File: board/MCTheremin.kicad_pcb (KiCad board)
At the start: 2 copper layers, 100 x 100 mm, 94 parts, among them J1 Barrel_Jack, J11 Conn_01x01, J12 Conn_01x01, J14 Conn_01x01, J15 Conn_01x01, J2 Conn_01x02, J21 DIN-5_180degree, J3 AudioJack2_Dual_Ground_Switch, J4 AudioJack2_Dual_Ground_Switch, J5 Conn_01x02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

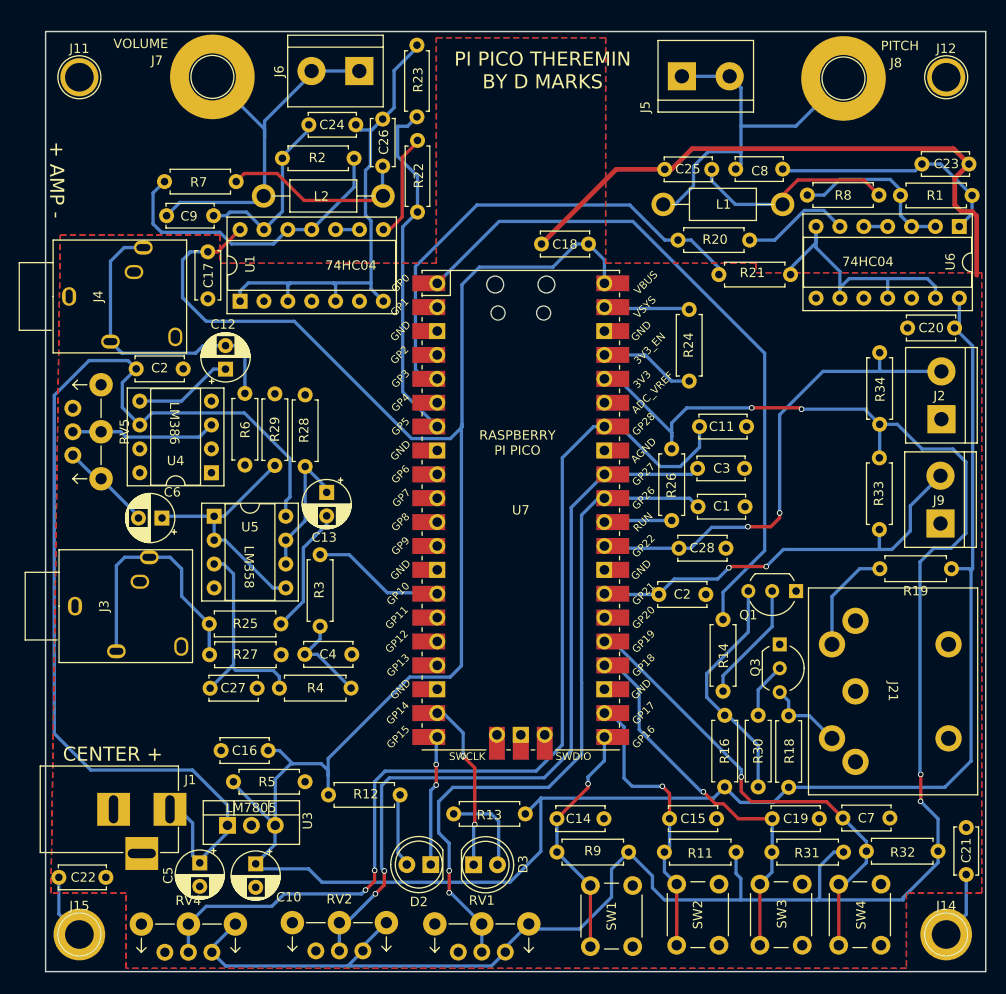
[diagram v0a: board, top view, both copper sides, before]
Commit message: Added external inductor support
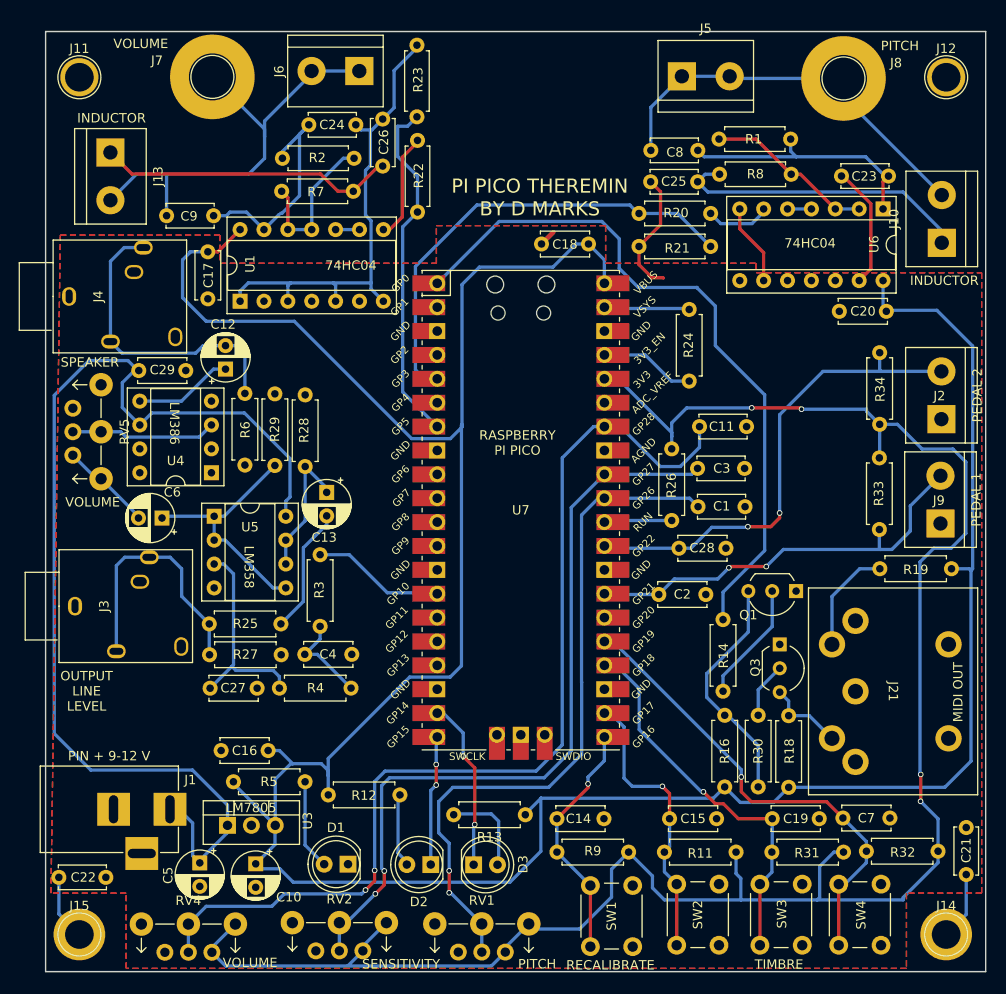
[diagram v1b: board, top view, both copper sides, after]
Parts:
- removed the C2 at (59.6, 85.9)
- removed L1, L2: 400 uH, Inductors_THT:L_Axial_L7.0mm_D3.3mm_P12.70mm_Horizontal_Fastron_MICC
- added C29: 100 nF, Capacitor_THT:C_Disc_D5.0mm_W2.5mm_P5.00mm, F.Cu at (59.9, 86.1)
- added D1: LED, LED_THT:LED_D5.0mm, F.Cu at (82.2, 138.6)
- added J10: Conn_01x02, TerminalBlock:TerminalBlock_bornier-2_P5.08mm, F.Cu at (145.3, 72.5)
- added J13: Conn_01x02, TerminalBlock:TerminalBlock_bornier-2_P5.08mm, F.Cu at (56.9, 62.9)
- J5: footprint Connectors_Terminal_Blocks:TerminalBlock_bornier-2_P5.08mm -> TerminalBlock:TerminalBlock_bornier-2_P5.08mm
- R12, R13, R5: footprint Resistors_THT:R_Axial_DIN0207_L6.3mm_D2.5mm_P7.62mm_Horizontal -> Resistor_THT:R_Axial_DIN0207_L6.3mm_D2.5mm_P7.62mm_Horizontal
- moved R1 20.2 mm to (121.6, 61.4)
- moved R7 12.5 mm to (75.1, 67.0)
- moved C8 9.25 mm to (119.4, 62.6)
- moved U6 8.32 mm to (139.1, 68.9)
- moved C20 7.47 mm to (139.4, 79.8)
- moved R20 5.03 mm to (120.7, 69.4)
- moved C23 3.78 mm to (139.7, 65.4), turned to 180 degrees
- moved R21 3.12 mm to (120.7, 72.9), turned to 180 degrees
- moved R8 2.80 mm to (129.3, 65.2), turned to 180 degrees
- moved C25 2.00 mm to (114.4, 66.0)
- moved R13 0.09 mm to (101.0, 133.3)
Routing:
- net GND: track 145.2 -> 88.5 mm
- net Net-(R2-Pad1): track 32.9 -> 17.0 mm
- net Net-(J13-Pin_1): track 20.6 -> 31.8 mm
- net Net-(J10-Pin_1): track 22.4 -> 32.1 mm
- net Net-(D1-A): track 0.00 -> 9.61 mm
- net +5V: track 299.5 -> 307.6 mm
- net Net-(J13-Pin_2): track 40.3 -> 47.8 mm
- net Net-(R20-Pad1): track 11.6 -> 6.92 mm
- net Net-(C24-Pad1): track 19.4 -> 24.0 mm
- net Net-(J10-Pin_2): track 40.5 -> 43.3 mm
- net PITCHSIG: track 52.2 -> 49.6 mm
- net MIDIOUT: track 73.5 -> 75.2 mm
- net Net-(C23-Pad1): track 25.8 -> 27.3 mm
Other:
- board text added: "INDUCTOR"
- board text added: "MIDI OUT"
- board text added: "OUTPUT LINE LEVEL"
- board text added: "PEDAL 1"
- board text added: "PEDAL 2"
- board text added: "PIN + 9-12 V"
- board text added: "RECALIBRATE"
- board text added: "SENSITIVITY"
- board text added: "SPEAKER"
- board text added: "TIMBRE"
- board text removed: "+ AMP -"
- board text removed: "CENTER +"

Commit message: Fixed layout
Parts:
- added R10: 2k, Resistor_THT:R_Axial_DIN0207_L6.3mm_D2.5mm_P7.62mm_Horizontal, F.Cu at (81.2, 82.9)
- added R15: 2k, Resistor_THT:R_Axial_DIN0207_L6.3mm_D2.5mm_P7.62mm_Horizontal, F.Cu at (84.4, 82.9)
- added R17: 1k, Resistor_THT:R_Axial_DIN0207_L6.3mm_D2.5mm_P7.62mm_Horizontal, F.Cu at (81.2, 100.5)
- added R35: 1k, Resistor_THT:R_Axial_DIN0207_L6.3mm_D2.5mm_P7.62mm_Horizontal, F.Cu at (81.9, 110.7)
- added R36: 1k, Resistor_THT:R_Axial_DIN0207_L6.3mm_D2.5mm_P7.62mm_Horizontal, F.Cu at (81.0, 120.6)
- added R37: 2k, Resistor_THT:R_Axial_DIN0207_L6.3mm_D2.5mm_P7.62mm_Horizontal, F.Cu at (84.4, 92.8)
- added R38: 2k, Resistor_THT:R_Axial_DIN0207_L6.3mm_D2.5mm_P7.62mm_Horizontal, F.Cu at (85.0, 103.1)
- added R39: 2k, Resistor_THT:R_Axial_DIN0207_L6.3mm_D2.5mm_P7.62mm_Horizontal, F.Cu at (84.2, 120.6)
- C27, C4: value 100 nF -> 10 nF
- R3, R4: value 10k -> 1k
- moved C4 8.73 mm to (71.5, 122.6), turned to 180 degrees
- moved R4 8.33 mm to (74.2, 119.4)
- moved R3 7.07 mm to (77.8, 112.6)
- moved R28 5.88 mm to (78.0, 90.4)
- moved R29 5.72 mm to (74.7, 90.5)
- moved C13 5.69 mm to (75.3, 95.7), turned to 0 degrees
- moved C27 3.31 mm to (64.2, 119.4), turned to 180 degrees
- moved C9 1.58 mm to (66.3, 69.7), turned to 90 degrees
- moved C2 0.94 mm to (116.1, 109.7)
- moved U1 0.79 mm to (69.9, 78.7)
- moved C17 0.60 mm to (66.7, 73.3)
- moved C16 0.12 mm to (73.8, 126.6)
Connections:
- C23 pad 1: Net-(C23-Pad1) -> Net-(J10-Pin_2)
- C24 pad 1: Net-(C24-Pad1) -> Net-(J13-Pin_2)
- C8 pad 1: Net-(C23-Pad1) -> Net-(J10-Pin_2)
- C8 pad 2: Net-(J10-Pin_2) -> Net-(J5-Pin_1)
- C9 pad 1: Net-(C24-Pad1) -> Net-(J13-Pin_2)
- C9 pad 2: Net-(J13-Pin_2) -> Net-(J6-Pin_1)
- J5 pad 1: Net-(J10-Pin_2) -> Net-(J5-Pin_1)
- J5 pad 2: Net-(J10-Pin_2) -> Net-(J5-Pin_1)
- J6 pad 1: Net-(J13-Pin_2) -> Net-(J6-Pin_1)
- J6 pad 2: Net-(J13-Pin_2) -> Net-(J6-Pin_1)
- J7 pad 1: Net-(J13-Pin_2) -> Net-(J6-Pin_1)
- J8 pad 1: Net-(J10-Pin_2) -> Net-(J5-Pin_1)
- R1 pad 2: Net-(C23-Pad1) -> Net-(J10-Pin_2)
- R2 pad 2: Net-(C24-Pad1) -> Net-(J13-Pin_2)
- U1 pad 13: Net-(C24-Pad1) -> Net-(J13-Pin_2)
- U6 pad 1: Net-(C23-Pad1) -> Net-(J10-Pin_2)
- U7 pad 14: SNDOUT -> Net-(U7-GPIO10)
- U7 pad 15: unconnected-(U7-GPIO11-Pad15) -> Net-(U7-GPIO11)
- U7 pad 16: unconnected-(U7-GPIO12-Pad16) -> Net-(U7-GPIO12)
- U7 pad 17: unconnected-(U7-GPIO13-Pad17) -> Net-(U7-GPIO13)
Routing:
- net Net-(J6-Pin_1): track 0.00 -> 28.8 mm
- net Net-(J5-Pin_1): track 0.00 -> 28.5 mm
- net Net-(C23-Pad1): track 27.3 -> 0.00 mm
- net Net-(C24-Pad1): track 24.0 -> 0.00 mm
- net Net-(U7-GPIO10): track 0.00 -> 23.3 mm
- net Net-(U7-GPIO11): track 0.00 -> 16.5 mm
- net Net-(R17-Pad1): track 0.00 -> 11.9 mm
- net Net-(R10-Pad2): track 0.00 -> 11.8 mm
- net Net-(R35-Pad1): track 0.00 -> 11.6 mm
- net Net-(J10-Pin_2): track 43.3 -> 33.8 mm
- net Net-(U7-GPIO13): track 0.00 -> 9.30 mm
- net Net-(U7-GPIO12): track 0.00 -> 8.42 mm
- net +9V: track 115.3 -> 123.0 mm
- net Net-(U5A--): track 26.6 -> 32.8 mm
- net Net-(C13-Pad2): track 13.5 -> 19.2 mm
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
